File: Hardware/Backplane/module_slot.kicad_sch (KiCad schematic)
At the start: 36 parts, among them J401 Conn_01x10, J402 10018784-10201TLF, J403 Conn_01x06, Q401 S3134K, Q402 GSF3407, Q403 GSF3407, Q404 GSF3407, U401 NL17SZS11DFT2G-Q

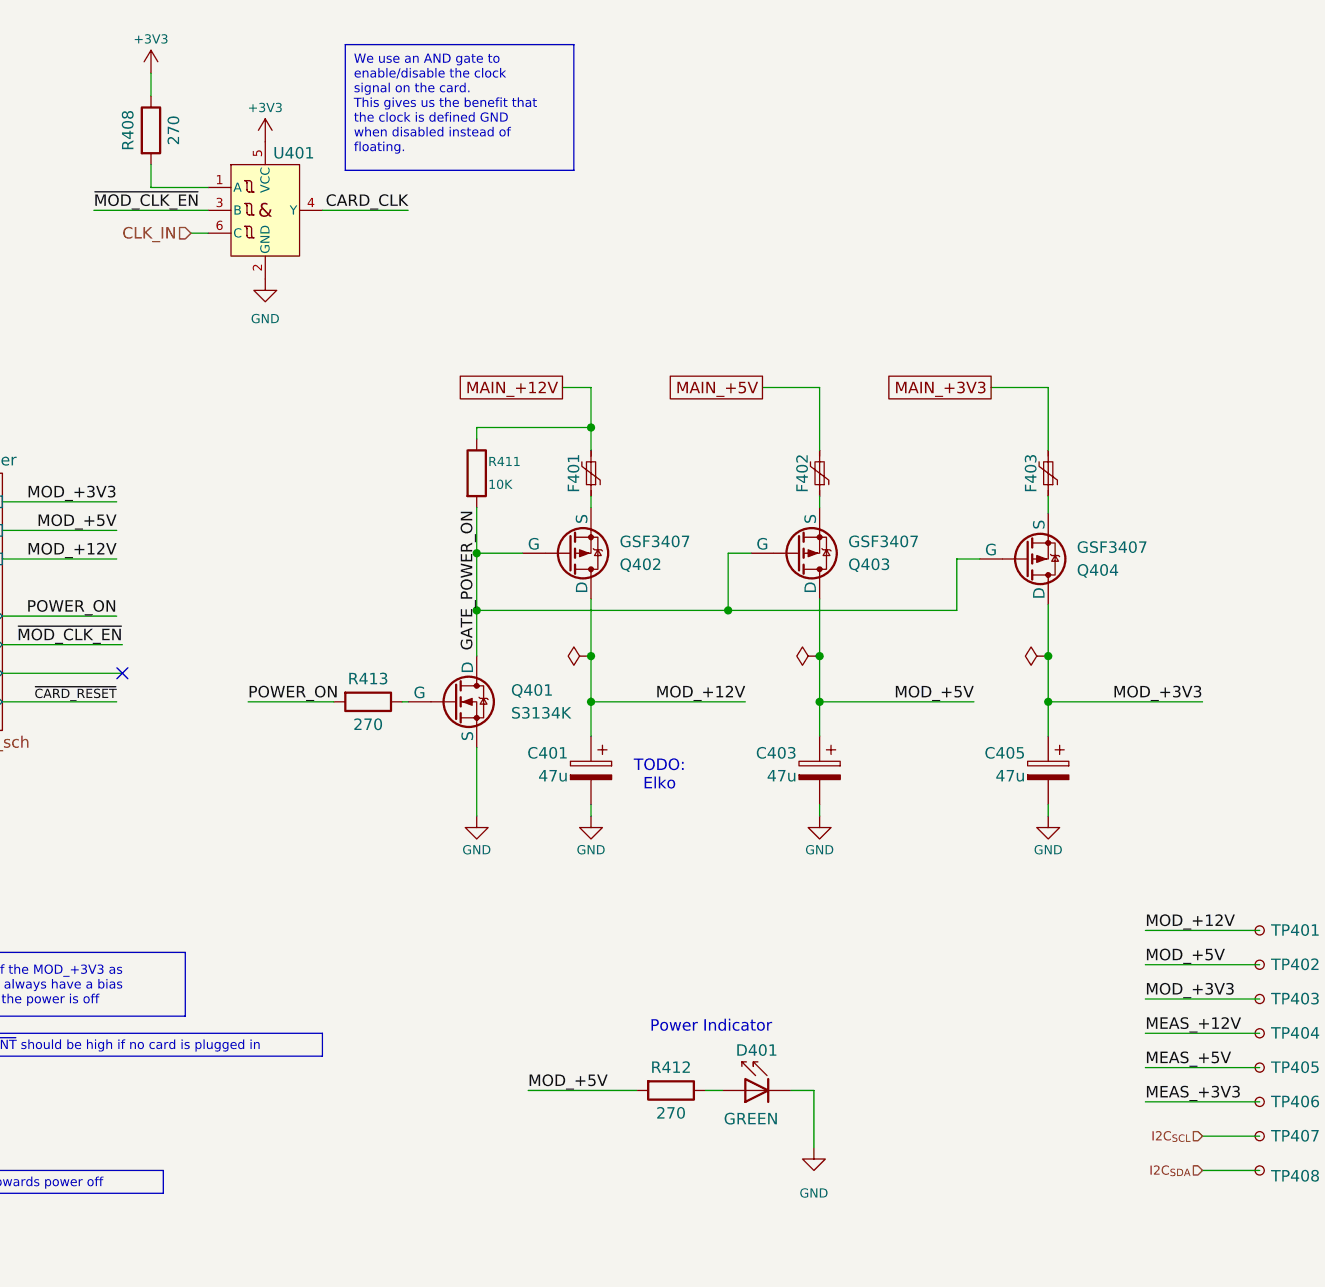
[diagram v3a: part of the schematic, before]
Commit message: Cleans up schematic even more, consolidates 270 and 100 Ohm resistors into the 560 ohm resistor, as they were only used as series resistors for the mosfets and LED current limiters
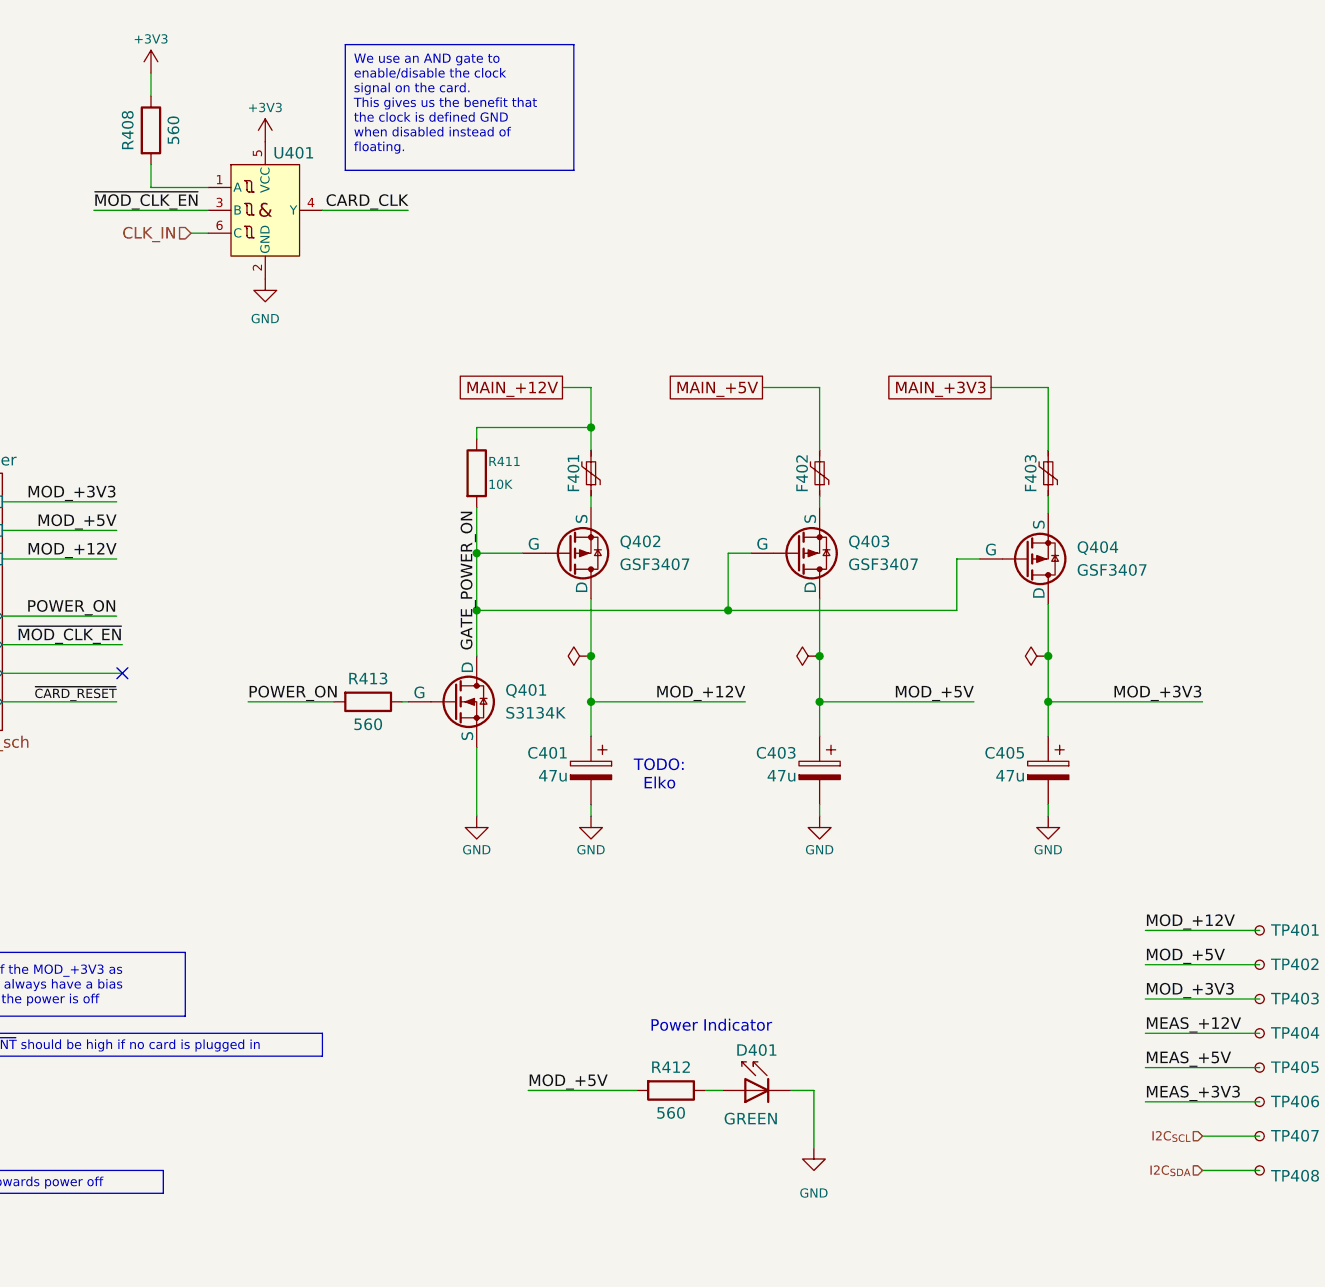
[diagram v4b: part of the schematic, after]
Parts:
- Q401: footprint (none) -> Package_TO_SOT_SMD:SOT-23; symbol Simulation_SPICE:NMOS -> Home Computer:S3134K
- Q402, Q403, Q404: footprint (none) -> Package_TO_SOT_SMD:SOT-23; symbol Simulation_SPICE:PMOS -> Home Computer:GSF3407
- R408, R412, R413: value 270 -> 560; Digikey Part No RMCF0603FT270RCT-ND -> RR08P560DCT-ND
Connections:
- net GATE_POWER_ON: now also Q401.3 (D), Q402.1 (G), Q403.1 (G), Q404.1 (G); no longer Q401.1 (D), Q402.2 (G), Q403.2 (G), Q404.2 (G)
- net GND: now also Q401.2 (S); no longer Q401.3 (S)
- net MOD_+12V: now also Q402.3 (D); no longer Q402.1 (D)
- net MOD_+3V3: now also Q404.3 (D); no longer Q404.1 (D)
- net MOD_+5V: now also Q403.3 (D); no longer Q403.1 (D)
- net at R413.1: now also Q401.1 (G); no longer Q401.2 (G)
- net at F403.1: now also Q404.2 (S); no longer Q404.3 (S)
- net at F402.1: now also Q403.2 (S); no longer Q403.3 (S)
- net at F401.1: now also Q402.2 (S); no longer Q402.3 (S)
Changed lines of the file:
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@@
 			)
 		)
-		(property "Value" "270"
+		(property "Value" "560"
 			(at 152.4 25.4 90)
 			(effects
@@
 			)
 		)
-		(property "Datasheet" "https://www.seielect.com/catalog/SEI-RMCF_RMCP.pdf"
+		(property "Datasheet" "https://www.susumu.co.jp/common/pdf/n_catalog_partition05_en.pdf"
 			(at 149.86 25.4 0)
 			(effects
@@
 			)
 		)
-		(property "Digikey Part No" "RMCF0603FT270RCT-ND"
+		(property "Digikey Part No" "RR08P560DCT-ND"
 			(at 149.86 25.4 90)
 			(effects
@@
 			)
 		)
-		(property "Value" "270"
+		(property "Value" "560"
 			(at 173.99 91.44 90)
 			(effects
@@
 			)
 		)
-		(property "Datasheet" "https://www.seielect.com/catalog/SEI-RMCF_RMCP.pdf"
+		(property "Datasheet" "https://www.susumu.co.jp/common/pdf/n_catalog_partition05_en.pdf"
 			(at 173.99 88.9 0)
 			(effects
@@
 			)
 		)
-		(property "Digikey Part No" "RMCF0603FT270RCT-ND"
+		(property "Digikey Part No" "RR08P560DCT-ND"
 			(at 173.99 88.9 90)
 			(effects
@@
 	)
 	(symbol
-		(lib_id "Simulation_SPICE:PMOS")
-		(at 247.015 73.025 0)
+		(lib_id "Home Computer:GSF3407")
+		(at 249.555 73.025 0)
 		(mirror x)
 		(unit 1)
@@
 		(fields_autoplaced yes)
 		(property "Reference" "Q404"
-			(at 252.73 74.2951 0)
+			(at 252.73 71.7549 0)
 			(effects
 				(font
@@
 		)
 		(property "Value" "GSF3407"
-			(at 252.73 71.7551 0)
+			(at 252.73 74.2949 0)
 			(effects
 				(font
@@
 			)
 		)
-		(property "Footprint" ""
-			(at 252.095 75.565 0)
+		(property "Footprint" "Package_TO_SOT_SMD:SOT-23"
+			(at 272.415 89.789 0)
 			(effects
 				(font
@@
 		)
 		(property "Datasheet" "https://goodarksemi.com/docs/datasheets/mosfets/GSF3407.pdf"
-			(at 247.015 60.325 0)
+			(at 243.205 92.329 0)
 			(effects
 				(font
@@
 		)
 		(property "Description" "30V P-Channel MOSFET"
-			(at 247.015 73.025 0)
+			(at 270.383 60.325 0)
 			(effects
 				(font
@@
 		)
 		(property "Digikey Part No" "4786-GSF3407CT-ND"
-			(at 247.015 73.025 0)
+			(at 249.555 73.025 0)
 			(effects
 				(font
@@
 		(pin "1"
 		)
-		(pin "3"
-		)
 		(pin "2"
 		)
+		(pin "3"
+		)
 		(instances
 			(project "Backplane"
@@
 	)
 	(symbol
-		(lib_id "Simulation_SPICE:NMOS")
-		(at 183.515 88.9 0)
+		(lib_id "Home Computer:S3134K")
+		(at 186.055 88.9 0)
 		(unit 1)
 		(exclude_from_sim no)
@@
 		(fields_autoplaced yes)
 		(property "Reference" "Q401"
-			(at 189.865 87.6299 0)
+			(at 189.23 87.6299 0)
 			(effects
 				(font
@@
 		)
 		(property "Value" "S3134K"
-			(at 189.865 90.1699 0)
+			(at 189.23 90.1699 0)
 			(effects
 				(font
@@
 			)
 		)
-		(property "Footprint" ""
-			(at 188.595 86.36 0)
+		(property "Footprint" "Package_TO_SOT_SMD:SOT-23"
+			(at 208.915 72.136 0)
 			(effects
 				(font
@@
 		)
 		(property "Datasheet" "https://goodarksemi.com/docs/datasheets/mosfets/S3134K.pdf"
-			(at 183.515 101.6 0)
+			(at 179.705 69.596 0)
 			(effects
 				(font
@@
 		)
 		(property "Description" "20V N-Channel MOSFET"
-			(at 183.515 88.9 0)
+			(at 206.883 101.6 0)
 			(effects
 				(font
@@
 		)
 		(property "Digikey Part No" "4786-S3134KCT-ND"
-			(at 183.515 88.9 0)
+			(at 186.055 88.9 0)
 			(effects
 				(font
-					(size 1.27 1.27)
+					(size 1.016 1.016)
 				)
 				(hide yes)
@@
 	)
 	(symbol
-		(lib_id "Simulation_SPICE:PMOS")
-		(at 221.615 72.39 0)
+		(lib_id "Home Computer:GSF3407")
+		(at 224.155 72.39 0)
 		(mirror x)
 		(unit 1)
@@
 		(fields_autoplaced yes)
 		(property "Reference" "Q403"
-			(at 227.33 73.6601 0)
+			(at 227.33 71.1199 0)
 			(effects
 				(font
@@
 		)
 		(property "Value" "GSF3407"
-			(at 227.33 71.1201 0)
+			(at 227.33 73.6599 0)
 			(effects
 				(font
@@
 			)
 		)
-		(property "Footprint" ""
-			(at 226.695 74.93 0)
+		(property "Footprint" "Package_TO_SOT_SMD:SOT-23"
+			(at 247.015 89.154 0)
 			(effects
 				(font
@@
 		)
 		(property "Datasheet" "https://goodarksemi.com/docs/datasheets/mosfets/GSF3407.pdf"
-			(at 221.615 59.69 0)
+			(at 217.805 91.694 0)
 			(effects
 				(font
@@
 		)
 		(property "Description" "30V P-Channel MOSFET"
-			(at 221.615 72.39 0)
+			(at 244.983 59.69 0)
 			(effects
 				(font
@@
 		)
 		(property "Digikey Part No" "4786-GSF3407CT-ND"
-			(at 221.615 72.39 0)
+			(at 224.155 72.39 0)
 			(effects
 				(font
@@
 	)
 	(symbol
-		(lib_id "Simulation_SPICE:PMOS")
-		(at 196.215 72.39 0)
+		(lib_id "Home Computer:GSF3407")
+		(at 198.755 72.39 0)
 		(mirror x)
 		(unit 1)
@@
 		(fields_autoplaced yes)
 		(property "Reference" "Q402"
-			(at 201.93 73.6601 0)
+			(at 201.93 71.1199 0)
 			(effects
 				(font
@@
 		)
 		(property "Value" "GSF3407"
-			(at 201.93 71.1201 0)
+			(at 201.93 73.6599 0)
 			(effects
 				(font
@@
 			)
 		)
-		(property "Footprint" ""
-			(at 201.295 74.93 0)
+		(property "Footprint" "Package_TO_SOT_SMD:SOT-23"
+			(at 221.615 89.154 0)
 			(effects
 				(font
@@
 		)
 		(property "Datasheet" "https://goodarksemi.com/docs/datasheets/mosfets/GSF3407.pdf"
-			(at 196.215 59.69 0)
+			(at 192.405 91.694 0)
 			(effects
 				(font
@@
 		)
 		(property "Description" "30V P-Channel MOSFET"
-			(at 196.215 72.39 0)
+			(at 219.583 59.69 0)
 			(effects
 				(font
@@
 		)
 		(property "Digikey Part No" "4786-GSF3407CT-ND"
-			(at 196.215 72.39 0)
+			(at 198.755 72.39 0)
 			(effects
 				(font
@@
 			)
 		)
-		(pin "1"
-		)
 		(pin "3"
 		)
 		(pin "2"
 		)
+		(pin "1"
+		)
 		(instances
 			(project "Backplane"
@@
 			)
 		)
-		(property "Value" "270"
+		(property "Value" "560"
 			(at 207.645 134.62 90)
 			(effects
@@
 			)
 		)
-		(property "Datasheet" "https://www.seielect.com/catalog/SEI-RMCF_RMCP.pdf"
+		(property "Datasheet" "https://www.susumu.co.jp/common/pdf/n_catalog_partition05_en.pdf"
 			(at 207.645 132.08 0)
 			(effects
@@
 			)
 		)
-		(property "Digikey Part No" "RMCF0603FT270RCT-ND"
+		(property "Digikey Part No" "RR08P560DCT-ND"
 			(at 207.645 132.08 90)
 			(effects

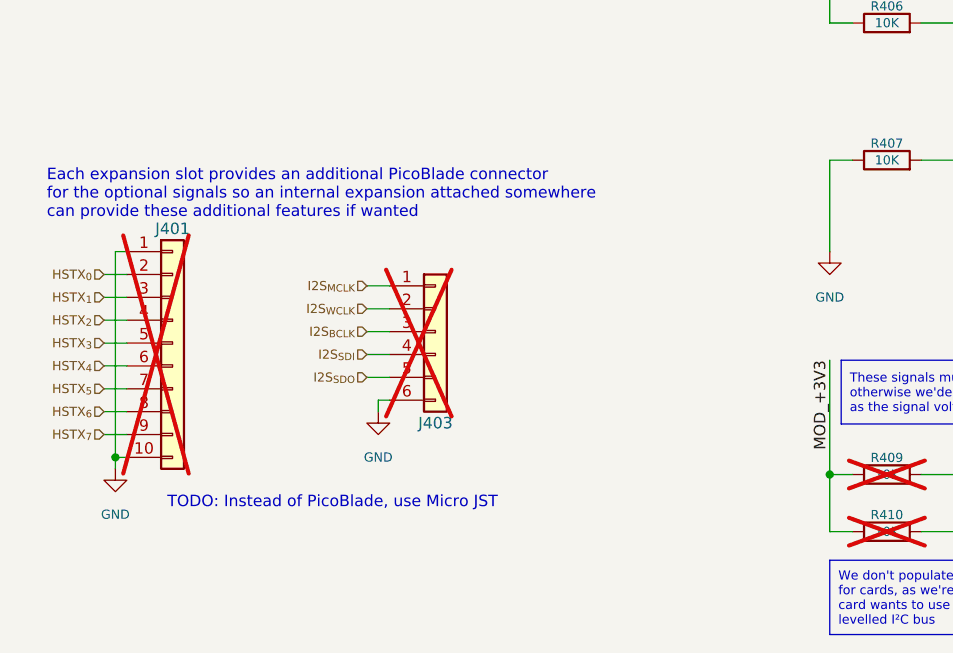
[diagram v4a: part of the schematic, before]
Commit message: More BOM consolidation
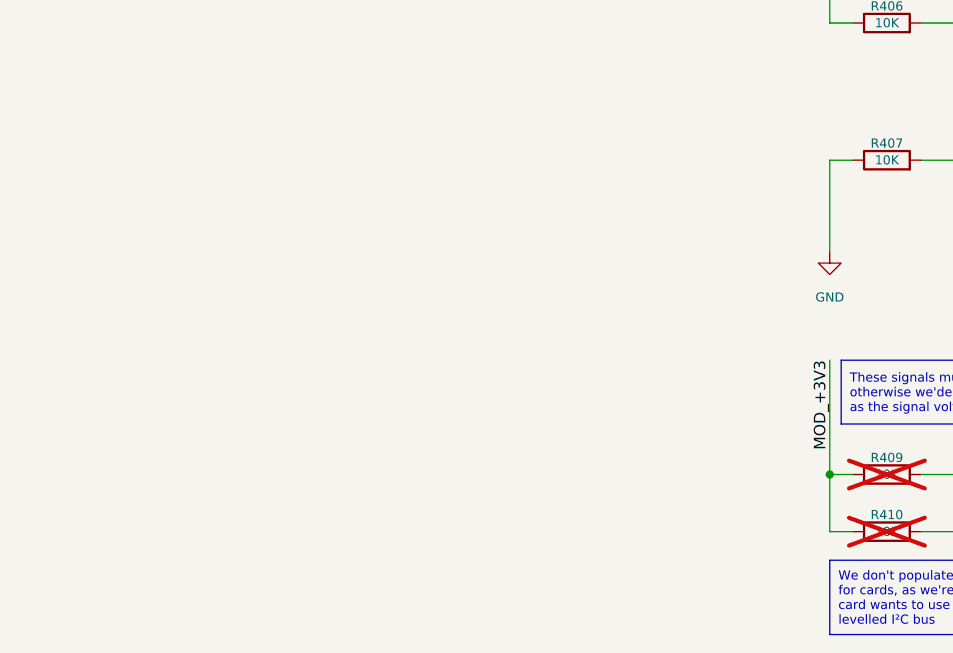
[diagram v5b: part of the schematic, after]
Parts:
- removed J401: Conn_01x10, Connector_Molex:Molex_PicoBlade_53047-1010_1x10_P1.25mm_Vertical, symbol Connector_Generic:Conn_01x10
- removed J403: Conn_01x06, Connector_Molex:Molex_PicoBlade_53047-0610_1x06_P1.25mm_Vertical, symbol Connector_Generic:Conn_01x06
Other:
- note removed: "Each expansion slot provides an additional PicoBlade connector for the optional signals so an internal expansion attached somewhere can provide these additional features if wanted"
- note removed: "TODO: Instead of PicoBlade, use Micro JST"

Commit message: Upgrades schematic files to KiCAD 10.0
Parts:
- U401: DigiKey Part No 488-NL17SZS11DFT2G-QCT-ND -> (none); Digikey Part No (none) -> 488-NL17SZS11DFT2G-QCT-ND

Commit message: Further backplane PCB cleanup.
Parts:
- removed TP404, TP405, TP406: TestPoint_Small, TestPoint:TestPoint_Pad_D1.0mm, symbol Connector:TestPoint_Small
- added R414: 10K, Resistor_SMD:R_0603_1608Metric, symbol Device:R_Small
- J402: symbol Home Computer:AHC-MODCONN-GEN1 Socket -> Home Computer:AHC-CONN-MOD
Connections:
- net MOD_+3V3: now also R414.1
- net at J402.A8 (MOD_SENSE): now also R414.2
- no-connect marks 10 -> 9

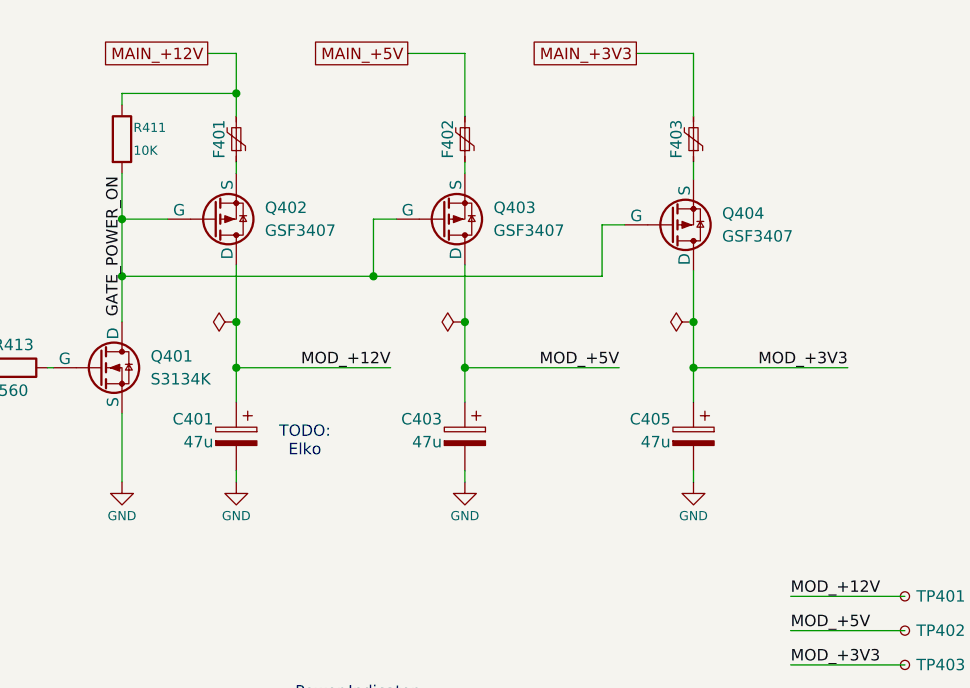
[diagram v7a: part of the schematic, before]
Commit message: Backplane: Fixes missing footprints/parts, starts to work on the layout seriously.
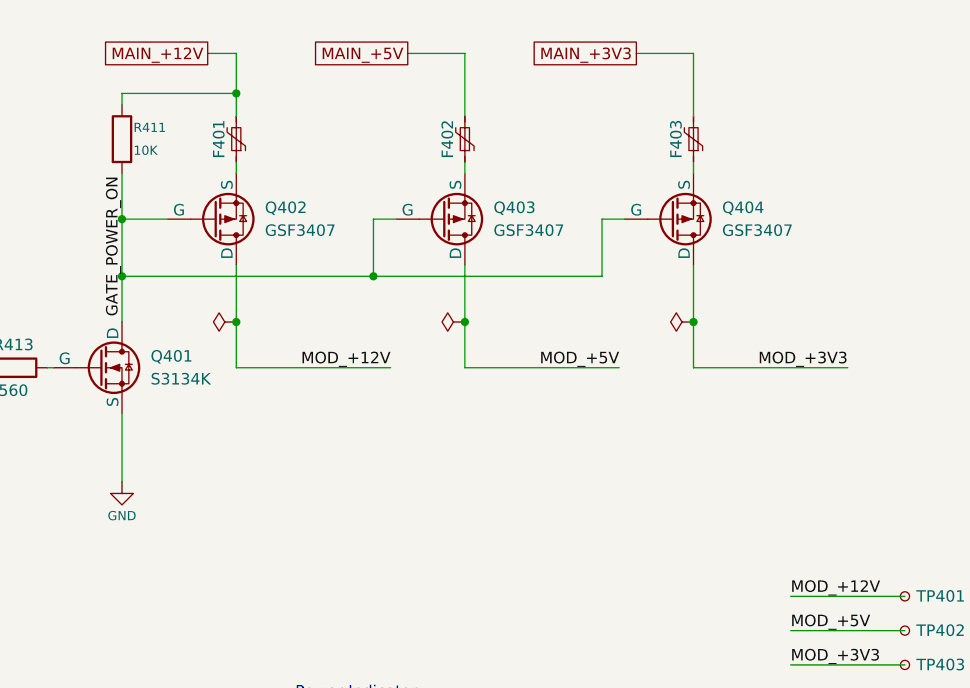
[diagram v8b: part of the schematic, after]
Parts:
- removed C401, C403, C405: 47u, Capacitor_SMD:C_0603_1608Metric, symbol Device:C_Polarized
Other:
- note removed: "TODO: Elko"
- moved on the sheet: Q404
